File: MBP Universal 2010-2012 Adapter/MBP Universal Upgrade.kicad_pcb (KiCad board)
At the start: 2 copper layers, 17 x 10 mm, 3 parts, among them J1 501745-0301, P1 Edge Connector

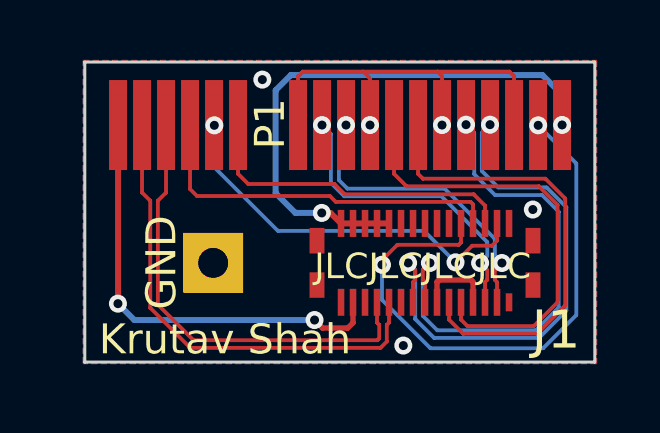
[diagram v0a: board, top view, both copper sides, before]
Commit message: Made large changes and fixes to the adapter
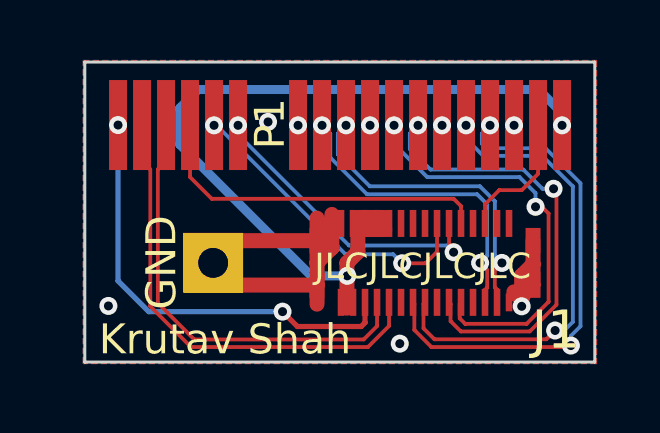
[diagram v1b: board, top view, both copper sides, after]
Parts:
- J1: value 501745-0301 -> Molex 501745-0301
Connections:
- net PCIE_AP_R2D_N renamed /PCIE_AP_R2D_N
- net PCIE_AP_R2D_P renamed /PCIE_AP_R2D_P
- net PCIE_CLK100M_AP_N renamed /PCIE_CLK100M_AP_N
- net PCIE_CLK100M_AP_P renamed /PCIE_CLK100M_AP_P
- J1 pad 10: WIFI_EVENT_L -> AP_CLKREQ_Q_L
- J1 pad 12: Net-(J1-Pad12) -> /AP_PCIE_WAKE_L
- J1 pad 14: Net-(J1-Pad14) -> AP_RESET_CONN_L
- J1 pad 18: GND -> Net-(J1-Pad18)
- J1 pad 2: GND -> Net-(J1-Pad2)
- J1 pad 20: GND -> Net-(J1-Pad20)
- J1 pad 25: GND -> PP3V3_S3_BT_F
- J1 pad 27: PP3V3_S3_BT_F -> PP3V3_WLAN
- J1 pad 30: PP3V3_WLAN -> GND
- J1 pad 4: AP_RESET_CONN_L -> Net-(J1-Pad4)
- J1 pad 6: AP_PCIE_WAKE_L -> WIFI_EVENT_L
- J1 pad 8: AP_CLKREQ_Q_L -> GND
- P1 pad 13: AP_PCIE_WAKE_L -> /AP_PCIE_WAKE_L
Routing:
- net WIFI_EVENT_L: track 19.3 -> 4.45 mm, vias 2 -> 0
- net AP_PCIE_WAKE_L: track 10.9 -> 0.00 mm
- net /AP_PCIE_WAKE_L: track 0.00 -> 10.1 mm, vias 0 -> 2
- net PP3V3_WLAN: track 18.7 -> 26.9 mm
- net AP_RESET_CONN_L: track 13.0 -> 10.4 mm
- net /PCIE_AP_R2D_P: track 16.6 -> 15.4 mm
- net /PCIE_AP_R2D_N: track 17.5 -> 16.5 mm
- net /PCIE_CLK100M_AP_P: track 15.0 -> 14.1 mm, vias 0 -> 2
- net AP_CLKREQ_Q_L: track 12.4 -> 11.7 mm
- net PCIE_AP_D2R_N: track 10.3 -> 10.9 mm
- net /PCIE_CLK100M_AP_N: track 15.5 -> 15.1 mm, vias 0 -> 2
- net GND: track 16.9 -> 16.8 mm, vias 5 -> 8

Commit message: Matched trace lengths
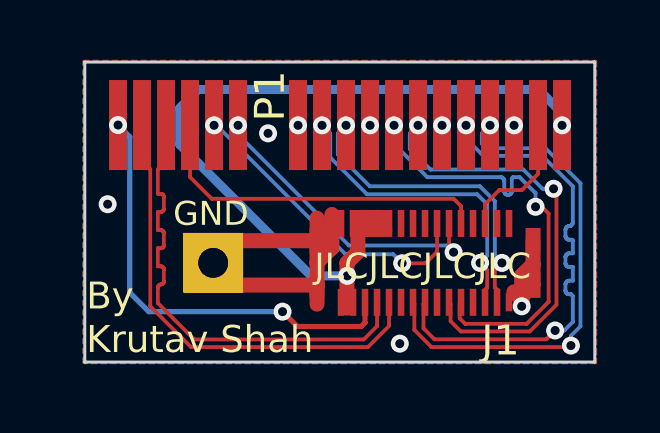
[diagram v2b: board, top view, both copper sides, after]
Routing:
- net /PCIE_AP_R2D_P: track 15.4 -> 16.5 mm
- net /PCIE_CLK100M_AP_P: track 14.1 -> 15.1 mm
- net USB_BT_N: track 15.1 -> 16.0 mm
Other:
- board text added: "By Krutav Shah"
- board text added: "Version 1.1"
- board text removed: "Krutav Shah"
